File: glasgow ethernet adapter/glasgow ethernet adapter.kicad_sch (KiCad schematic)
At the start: 49 parts, among them J1 Glasgow Port, J2 RJ45_Amphenol_RJMG1S8008101BR, U1 MxL86110, Y1 25 MHz

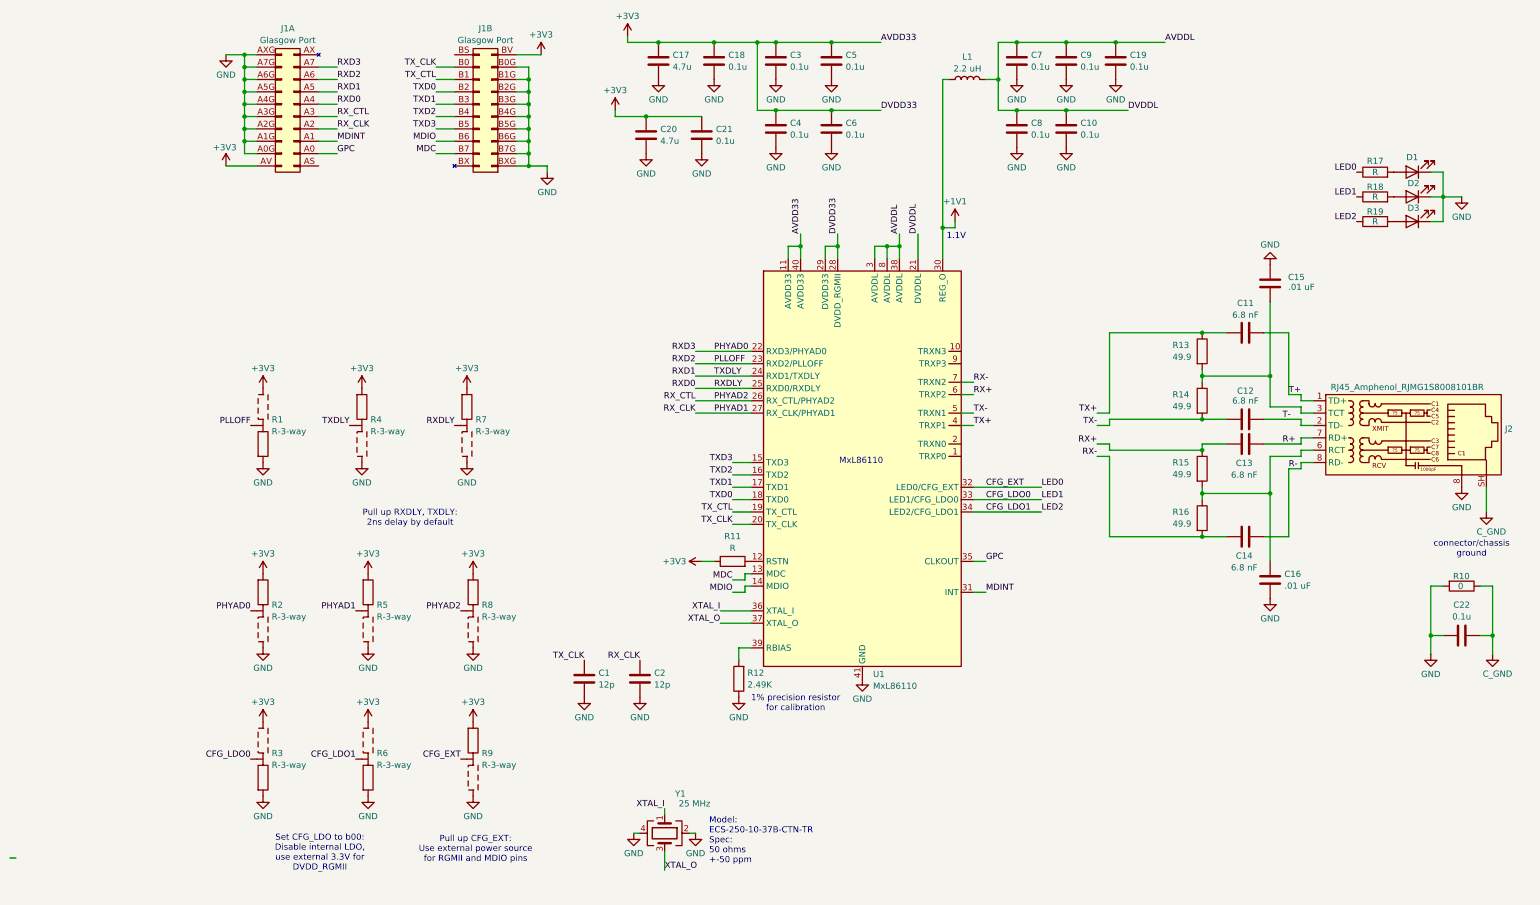
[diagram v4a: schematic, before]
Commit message: wip - add 4-pair RJ45, switch to 4 layers
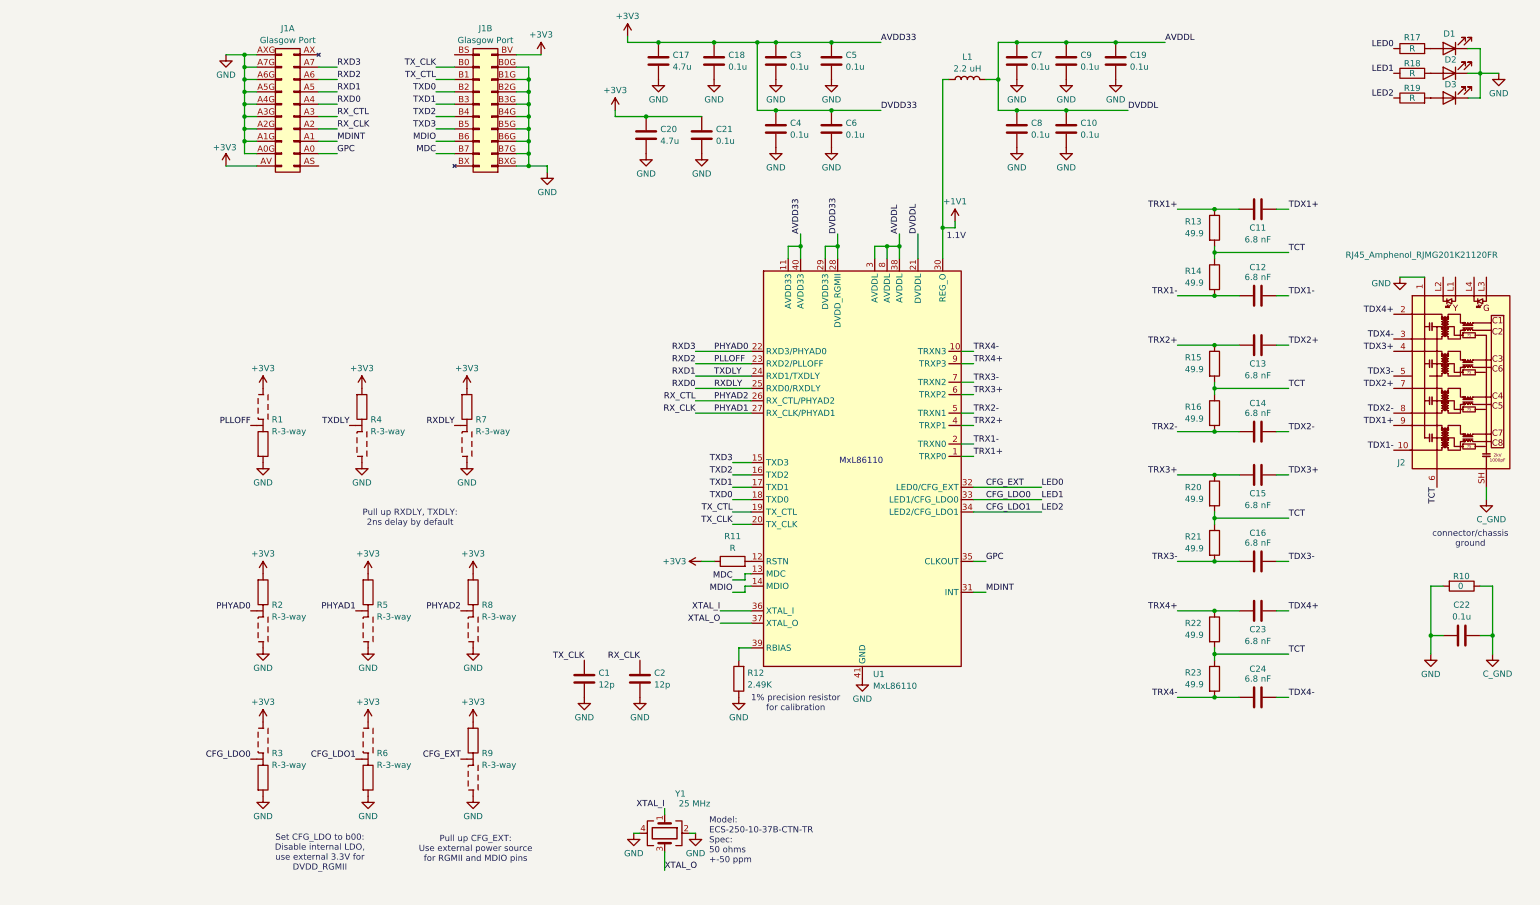
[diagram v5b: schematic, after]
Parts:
- removed J2: RJ45_Amphenol_RJMG1S8008101BR, glasgow:AMPHENOL_RJMG1S8008101BR, symbol glasgow:RJ45_Amphenol_RJMG1S8008101BR
- added C23, C24: 6.8 nF, Capacitor_SMD:C_0402_1005Metric, symbol Device:C
- added J2: RJ45_Amphenol_RJMG201K21120FR, glasgow:AMPHENOL_RJMG201K21120FR, symbol glasgow:RJ45_Amphenol_RJMG201K21120FR
- added R20, R21, R22, R23: 49.9, Resistor_SMD:R_0402_1005Metric, symbol Device:R
- C11, C12, C13, C14: footprint Capacitor_SMD:C_0603_1608Metric -> Capacitor_SMD:C_0402_1005Metric
- C15, C16: value .01 uF -> 6.8 nF; footprint Capacitor_SMD:C_0603_1608Metric -> Capacitor_SMD:C_0402_1005Metric
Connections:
- net C_GND: now also J2.SH
- net GND: now also J2.1 (GND); no longer C15.2, C16.2
- net TCT: now reaches R15.2, R16.1
- net TCT: now also R13.2, R14.1, J2.6 (TCT), R20.2, R21.1, R22.2, R23.1; no longer C16.1
- net TRX1+: now reaches U1.1 (TRXP0)
- net TRX1+: now also C11.2, R13.1
- net TRX4-: now reaches U1.10 (TRXN3)
- net TRX4-: now also C24.2, R23.2
- net TRX1-: now reaches U1.2 (TRXN0)
- net TRX1-: now also C12.2, R14.2
- net TRX4+: now reaches U1.9 (TRXP3)
- net TRX4+: now also C23.2, R22.1
- net R+ renamed TDX2+
- net TDX2+: now also J2.7 (TD3+)
- net R- renamed TDX2-
- net TDX2-: now also J2.8 (TD3-)
- net RX+ renamed TRX2+
- net TRX2+: now also U1.4 (TRXP1); no longer U1.6 (TRXP2)
- net RX- renamed TRX2-
- net TRX2-: now also U1.5 (TRXN1); no longer U1.7 (TRXN2)
- net T+ renamed TDX1+
- net TDX1+: now also J2.9 (TD4+)
- net T- renamed TDX1-
- net TDX1-: now also J2.10 (TD4-)
- removed net TX+: C11.2, R13.1, U1.4 (TRXP1)
- removed net TX-: C12.2, R14.2, U1.5 (TRXN1)
- new net TDX3+: C15.1, J2.4 (TD2+)
- new net TDX3-: C16.1, J2.5 (TD2-)
- new net TDX4+: C23.1, J2.2 (TD1+)
- new net TDX4-: C24.1, J2.3 (TD1-)
- new net TRX3+: C15.2, R20.1, U1.6 (TRXP2)
- new net TRX3-: C16.2, R21.2, U1.7 (TRXN2)
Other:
- moved on the sheet: C11, C12, D1, D2, D3, R13, R14, R17, R18, R19

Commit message: wip - add silkscreen
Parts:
- R1, R2, R3, R4, R5, R6, R7, R8, R9: value R-3-way -> 4.7k
- R11: value R -> 4.7k
- R17, R18, R19: value R -> 150
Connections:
- net +3V3: now also D1.2 (A)
- net GND: no longer D1.1 (K)
- net at R17.2: now also D1.1 (K); no longer D1.2 (A)
- no-connect marks 0 -> 4
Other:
- moved on the sheet: D1, D2, D3, R17, R18, R19

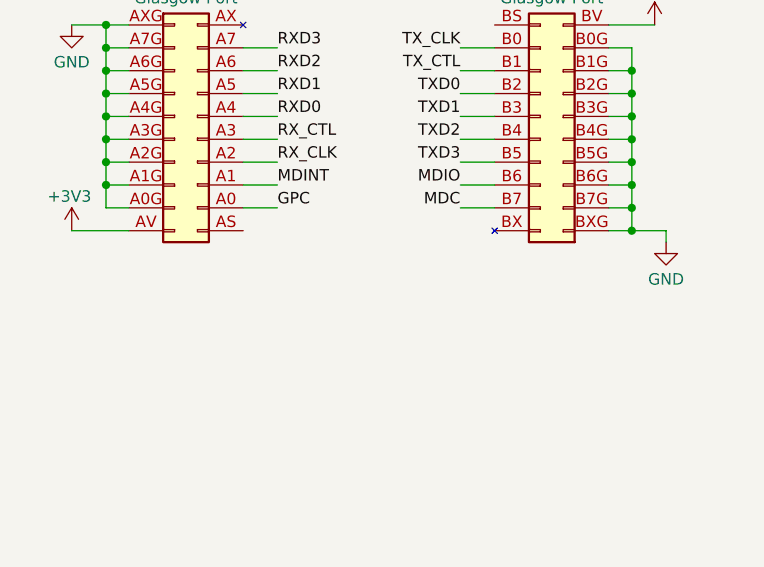
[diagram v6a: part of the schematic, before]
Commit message: length match RGMII traces
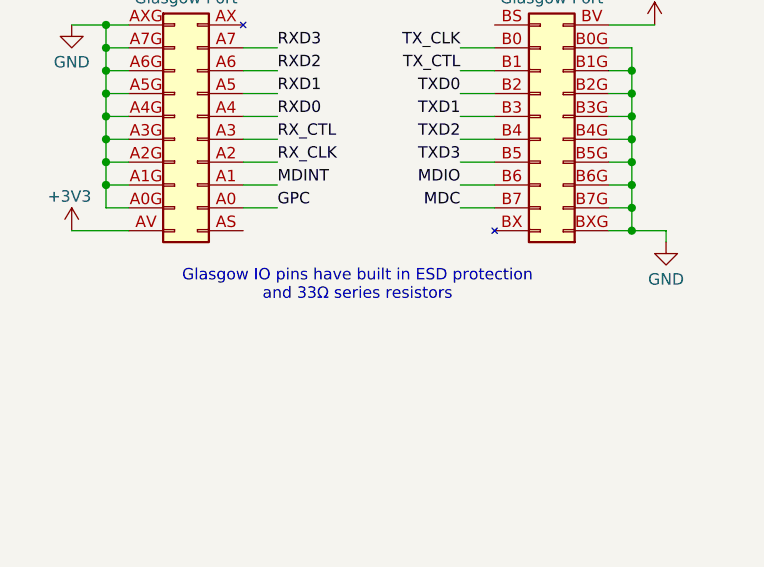
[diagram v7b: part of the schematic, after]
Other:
- note added: "Glasgow IO pins have built in ESD protection and 33Ω series resistors"
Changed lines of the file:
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@@
+		)
+	)
+	(text "Glasgow IO pins have built in ESD protection\nand 33Ω series resistors"
+		(exclude_from_sim no)
+		(at 50.8 51.816 0)
+		(effects
+			(font
+				(size 1.27 1.27)
+			)
 		)
 	)

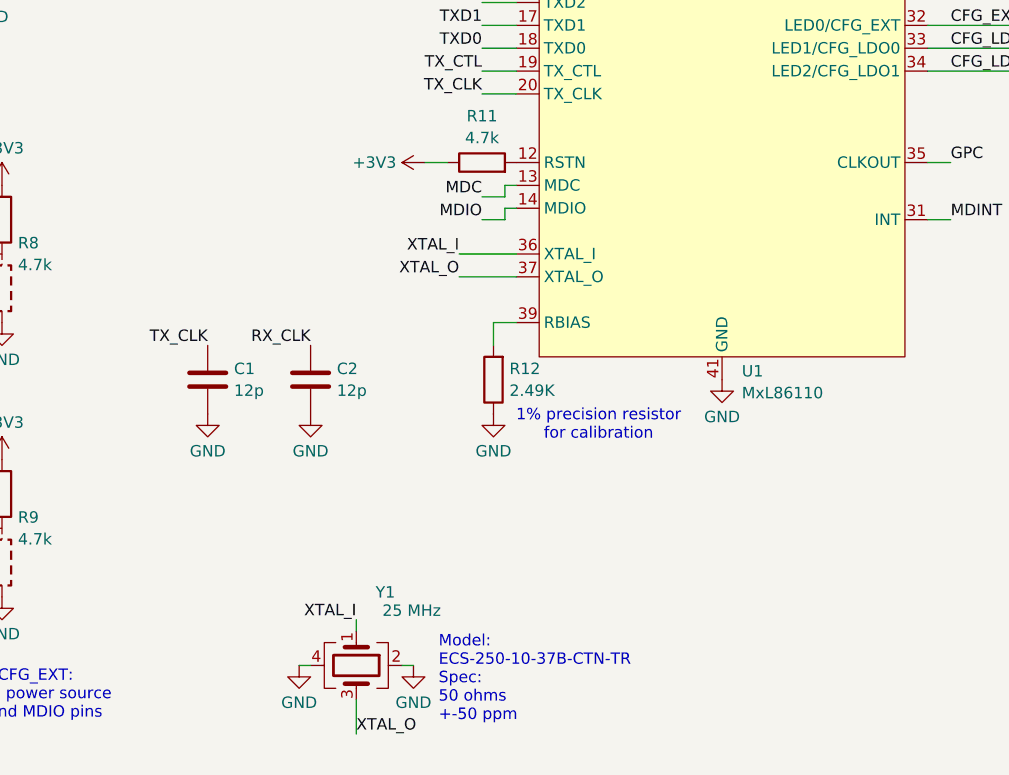
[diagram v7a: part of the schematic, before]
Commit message: add capacitors to crystal
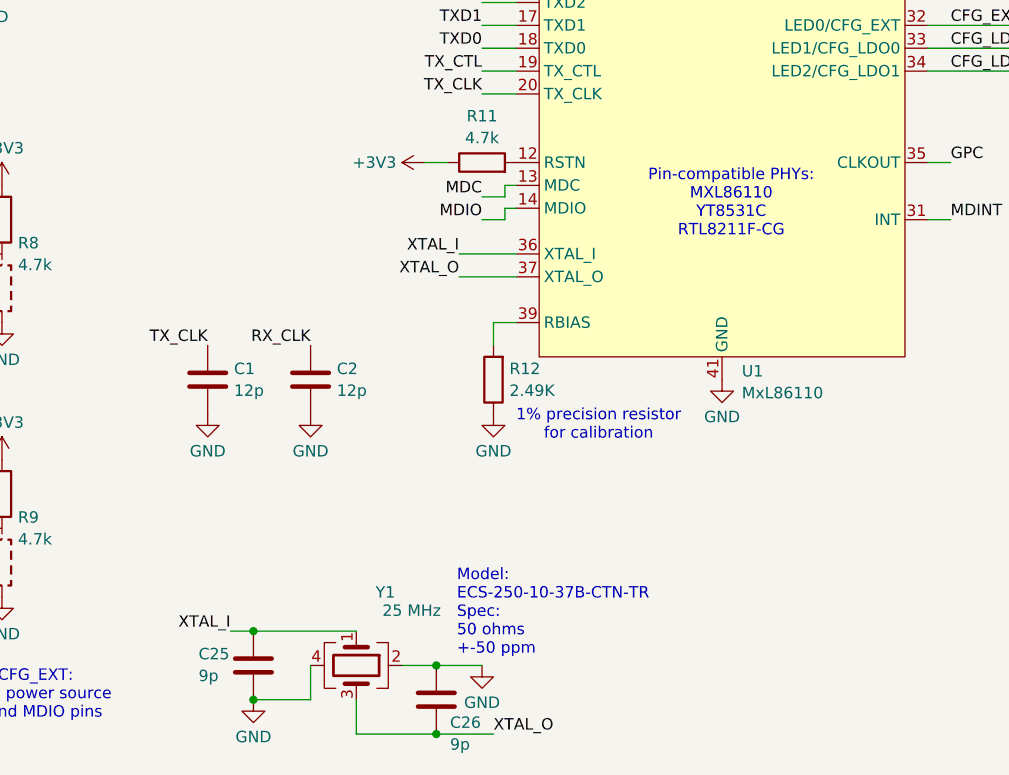
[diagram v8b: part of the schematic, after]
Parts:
- added C25, C26: 9p, Capacitor_SMD:C_0402_1005Metric, symbol Device:C
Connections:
- net GND: now also C25.2, C26.1
- net XTAL_I: now also C25.1
- net XTAL_O: now also C26.2
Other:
- note added: "Pin-compatible PHYs: MXL86110 YT8531C RTL8211F-CG"
